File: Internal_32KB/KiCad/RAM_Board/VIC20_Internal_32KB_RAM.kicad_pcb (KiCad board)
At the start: 2 copper layers, 65 x 61 mm, 13 parts, among them J1 UD4, J2 UE4, J3 Switch, J4 RAM Decode, J5 BLK Inputs, J6 BLK Outputs, U1 62256, U2 RAM Decoder, U3 BLK Decoder

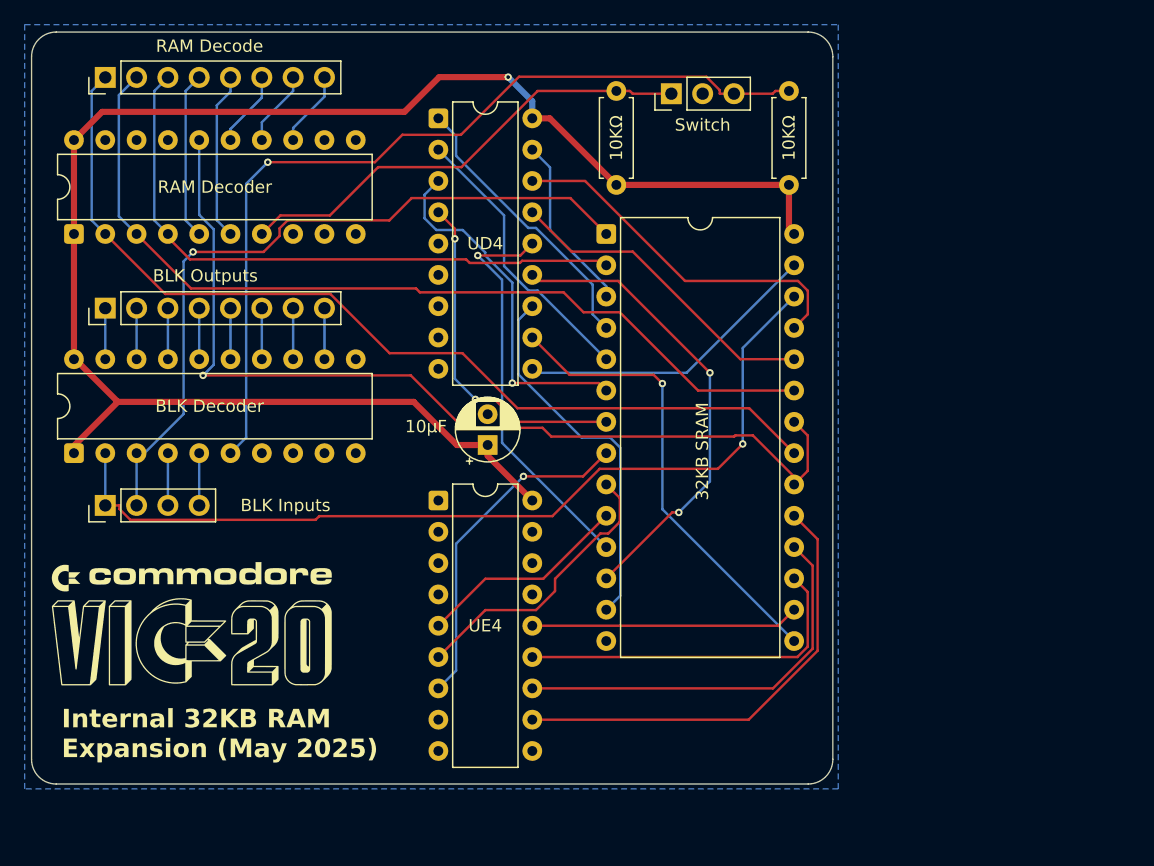
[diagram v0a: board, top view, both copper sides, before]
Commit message: Redesigned 32KB expansion
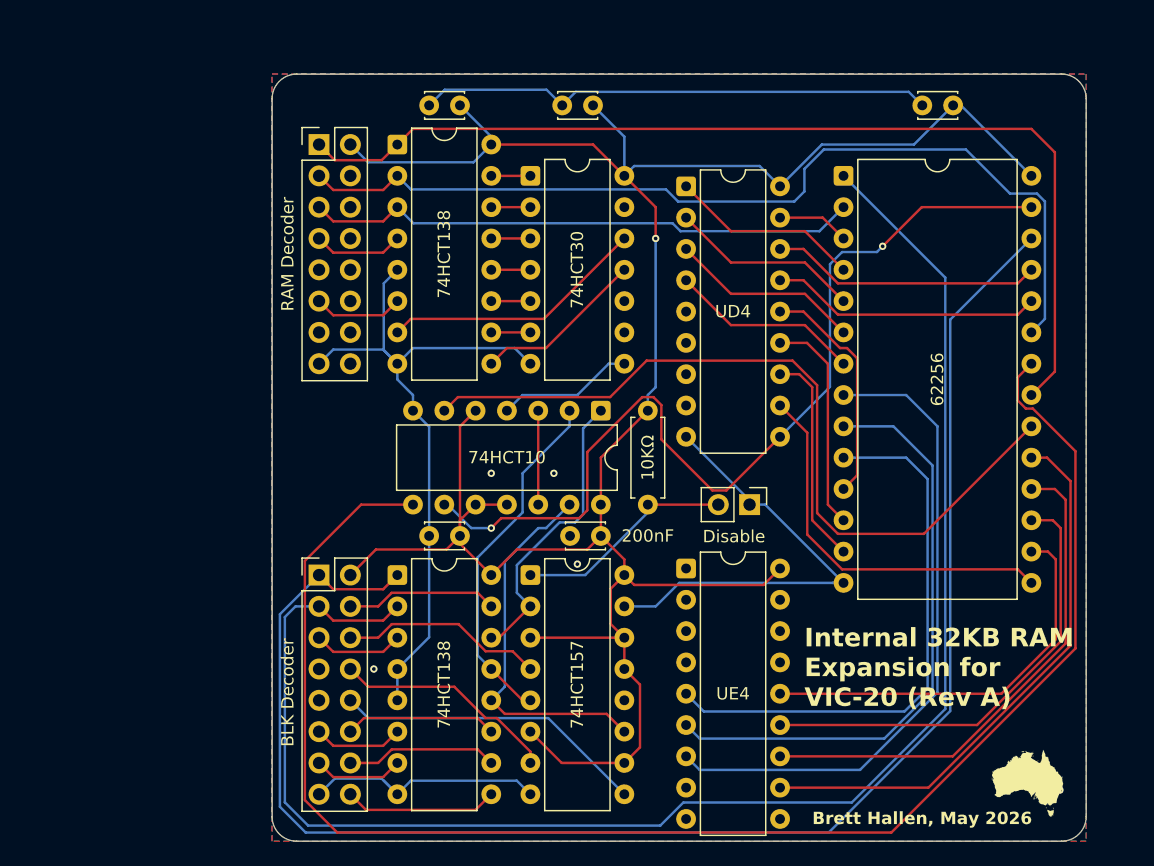
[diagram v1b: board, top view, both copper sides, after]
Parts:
- removed G***: LOGO, LOGO
- removed the J4 at (53.0, 31.8)
- removed the J5 at (53.0, 66.5)
- removed J6: BLK Outputs, Connector_PinHeader_2.54mm:PinHeader_1x08_P2.54mm_Vertical
- removed R2: 10KΩ, Resistor_THT:R_Axial_DIN0207_L6.3mm_D2.5mm_P7.62mm_Horizontal
- added C2: 100nF, Capacitor_THT:C_Disc_D3.0mm_W2.0mm_P2.50mm, F.Cu at (92.6, 34.1)
- added C3: 100nF, Capacitor_THT:C_Disc_D3.0mm_W2.0mm_P2.50mm, F.Cu at (121.8, 34.1)
- added C4: 100nF, Capacitor_THT:C_Disc_D3.0mm_W2.0mm_P2.50mm, F.Cu at (81.8, 69.0)
- added C5: 200nF, Capacitor_THT:C_Disc_D3.0mm_W2.0mm_P2.50mm, F.Cu at (93.2, 69.0)
- added J1: BLK Decoder, Connector_PinHeader_2.54mm:PinHeader_2x08_P2.54mm_Vertical, F.Cu at (70.4, 72.2)
- added J2: RAM Decoder, Connector_PinHeader_2.54mm:PinHeader_2x08_P2.54mm_Vertical, F.Cu at (70.4, 37.2)
- added U1: 74HCT138, Package_DIP:DIP-16_W7.62mm, F.Cu at (76.7, 72.2)
- added U4: 74HCT30, Package_DIP:DIP-14_W7.62mm, F.Cu at (87.5, 39.8)
- added U5: 74HCT157, Package_DIP:DIP-16_W7.62mm, F.Cu at (87.5, 72.2)
- C1: value 10µF -> 100nF; footprint Capacitor_THT:CP_Radial_D5.0mm_P2.50mm -> Capacitor_THT:C_Disc_D3.0mm_W2.0mm_P2.50mm
- J3: value Switch -> Disable/Enable Switch; footprint Connector_PinHeader_2.54mm:PinHeader_1x03_P2.54mm_Vertical -> Connector_PinHeader_2.54mm:PinHeader_1x02_P2.54mm_Vertical
- U2: value RAM Decoder -> 74HCT138; footprint Package_DIP:DIP-20_W7.62mm -> Package_DIP:DIP-16_W7.62mm
- U3: value BLK Decoder -> 74HCT10; footprint Package_DIP:DIP-20_W7.62mm -> Package_DIP:DIP-14_W7.62mm
- moved U3 42.9 mm to (93.2, 58.8), turned to -90 degrees
- moved J3 33.9 mm to (105.3, 66.5), turned to -90 degrees
- moved C1 27.6 mm to (81.8, 34.1), turned to 180 degrees
- moved U2 27.2 mm to (76.7, 37.2), turned to 0 degrees
- moved J4 20.8 mm to (100.1, 40.6)
- moved J5 20.8 mm to (100.1, 71.6)
- moved U6 19.8 mm to (112.9, 39.8)
- moved R1 18.5 mm to (97.0, 58.8), turned to -90 degrees
- renumbered J1 to J4, J2 to J5, U1 to U6
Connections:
- net BD0 renamed /BD0
- net BD1 renamed /BD1
- net BD2 renamed /BD2
- net BD3 renamed /BD3
- net BD4 renamed /BD4
- net BD5 renamed /BD5
- net BD6 renamed /BD6
- net BD7 renamed /BD7
- net VA0 renamed /VA0
- net VA1 renamed /VA1
- net VA2 renamed /VA2
- net VA3 renamed /VA3
- net VA4 renamed /VA4
- net VA5 renamed /VA5
- net VA6 renamed /VA6
- net VA7 renamed /VA7
- net VA8 renamed /VA8
- net VA9 renamed /VA9
- J3 pad 1: S1 -> GND
- J3 pad 2: GND -> Net-(J3-Pin_2)
- J4 pad 10: VR/W -> /VR/~{W}
- R1 pad 2: S1 -> Net-(J3-Pin_2)
- U2 pad 1: +5V -> /VA10
- U2 pad 10: GND -> /~{RAM5}
- U2 pad 11: GND -> /~{RAM4}
- U2 pad 12: unconnected-(U2-IO8-Pad12) -> /~{RAM3}
- U2 pad 13: ~{RAM3} -> /~{RAM2}
- U2 pad 14: ~{RAM2} -> /~{RAM1}
- U2 pad 15: ~{RAM1} -> /~{RAM0}
- U2 pad 16: ~{CS1} -> +5V
- U2 pad 2: VA10 -> /VA11
- U2 pad 3: VA11 -> /VA12
- U2 pad 4: VA12 -> /~{BLK0}/~{G2A}
- U2 pad 5: VA13/G1 -> GND
- U2 pad 6: ~{BLK0}/~{G2A} -> /VA13/G1
- U2 pad 7: S1 -> /~{RAM7}
- U2 pad 8: unconnected-(U2-I8-Pad8) -> GND
- U2 pad 9: unconnected-(U2-I9-Pad9) -> /~{RAM6}
- U3 pad 1: +5V -> /~{BLK1}
- U3 pad 10: GND -> +5V
- U3 pad 11: GND -> +5V
- U3 pad 12: ~{BLK7} -> /~{BLK_CS}
- U3 pad 13: ~{BLK6} -> /~{BLK3}
- U3 pad 14: ~{BLK5} -> +5V
- U3 pad 2: CA13 -> /~{BLK2}
- U3 pad 3: CA14 -> /~{BLK_CS}
- U3 pad 4: CA15 -> /~{RAM_CS}
- U3 pad 5: SΦ2/G1 -> +5V
- U3 pad 6: S2 -> /~{CS}
- U3 pad 7: unconnected-(U3-I7-Pad7) -> GND
- U3 pad 8: unconnected-(U3-I8-Pad8) -> /~{OE}
- U3 pad 9: unconnected-(U3-I9-Pad9) -> /VR/~{W}
- U6 pad 1: CA14 -> /CA14
- U6 pad 2: VA12 -> /VA12
- U6 pad 20: ~{CS1} -> /~{CS}
- U6 pad 21: VA10 -> /VA10
- U6 pad 22: ~{CS1} -> /~{OE}
- U6 pad 23: VA11 -> /VA11
- U6 pad 26: CA13 -> /CA13
- U6 pad 27: VR/W -> /VR/~{W}
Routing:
- net GND: track 0.00 -> 157.1 mm, vias 0 -> 5
- net /CA14: track 0.00 -> 130.4 mm
- net /CA13: track 0.00 -> 127.8 mm
- net /~{OE}: track 0.00 -> 125.7 mm
- net /VA10: track 0.00 -> 82.5 mm
- net ~{CS1}: track 77.8 -> 0.00 mm, vias 1 -> 0
- net VA10: track 76.9 -> 0.00 mm
- net /VA11: track 0.00 -> 76.3 mm
- net /VR/~{W}: track 0.00 -> 75.7 mm, vias 0 -> 2
- net CA13: track 72.8 -> 0.00 mm, vias 1 -> 0
- net VA11: track 72.5 -> 0.00 mm
- net S2: track 70.8 -> 0.00 mm, vias 1 -> 0
- net +5V: track 134.6 -> 199.5 mm
- net /~{CS}: track 0.00 -> 64.8 mm
- net CA14: track 60.0 -> 0.00 mm, vias 1 -> 0
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- added copper zone on F.Cu, net GND
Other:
- board size 65 x 61 mm -> 66 x 62.2 mm
- board text added: "26-MAY-2026: Pending testing"
- board text added: "Brett Hallen, May 2026"
- board text added: "Disable"
- board text added: "Internal 32KB RAM Expansion for VIC-20 (Rev A)"
- board text removed: "32KB SRAM"
- board text removed: "Brett Hallen, May 2025 Port Macquarie, Australia www.youtube.com/@Brfff"
- board text removed: "Internal 32KB RAM Expansion (May 2025)"

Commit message: Silkscreen improvements
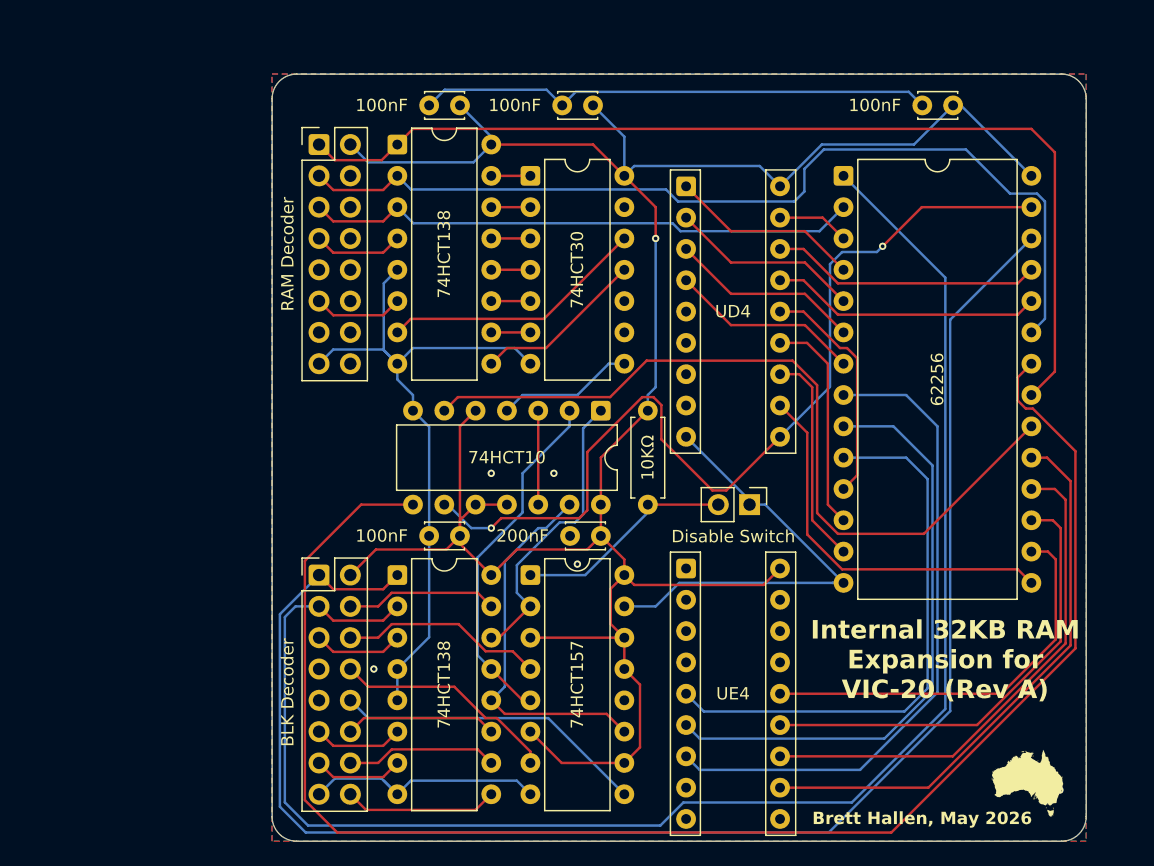
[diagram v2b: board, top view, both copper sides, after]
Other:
- board text added: "2114 SRAM Socket"
- board text added: "3-to-8 Decoder"
- board text added: "32KB SRAM"
- board text added: "8-Input NAND Gate"
- board text added: "Disable Switch"
- board text added: "Quad 2-Input Multiplexer"
- board text added: "To/From VIC"
- board text added: "Triple 3-Input NAND Gate"
- board text removed: "Disable"
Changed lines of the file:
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@@
 		)
 		(property "Value" "100nF"
-			(at 1.25 2.25 0)
-			(layer "F.Fab")
-			(hide yes)
+			(at 6.35 0 0)
+			(layer "F.SilkS")
 			(effects
 				(font
 					(size 1 1)
-					(thickness 0.15)
+					(thickness 0.125)
 				)
 			)
@@
 		)
 		(property "Value" "100nF"
-			(at 1.25 2.25 0)
-			(layer "F.Fab")
-			(hide yes)
+			(at 6.35 0 0)
+			(layer "F.SilkS")
 			(effects
 				(font
 					(size 1 1)
-					(thickness 0.15)
+					(thickness 0.125)
 				)
 			)
@@
 	)
 	(footprint "Package_DIP:DIP-18_W7.62mm"
-		(locked yes)
 		(layer "F.Cu")
 		(at 100.137 71.635)
@@
 		(attr through_hole)
 		(fp_line
+			(start -1.27 -1.33)
+			(end -1.27 21.65)
+			(stroke
+				(width 0.12)
+				(type solid)
+			)
+			(layer "F.SilkS")
+		)
+		(fp_line
+			(start 1.16 -1.33)
+			(end -1.27 -1.33)
+			(stroke
+				(width 0.12)
+				(type solid)
+			)
+			(layer "F.SilkS")
+		)
+		(fp_line
 			(start 1.16 -1.33)
 			(end 1.16 21.65)
@@
 		(fp_line
 			(start 1.16 21.65)
-			(end 6.46 21.65)
+			(end -1.27 21.65)
 			(stroke
 				(width 0.12)
@@
 		)
 		(fp_line
-			(start 2.81 -1.33)
-			(end 1.16 -1.33)
+			(start 6.46 21.65)
+			(end 6.46 -1.33)
 			(stroke
 				(width 0.12)
@@
 		)
 		(fp_line
-			(start 6.46 -1.33)
-			(end 4.81 -1.33)
+			(start 8.89 -1.33)
+			(end 6.46 -1.33)
 			(stroke
 				(width 0.12)
@@
 		)
 		(fp_line
-			(start 6.46 21.65)
-			(end 6.46 -1.33)
+			(start 8.89 21.65)
+			(end 6.46 21.65)
 			(stroke
 				(width 0.12)
@@
 			(layer "F.SilkS")
 		)
-		(fp_arc
-			(start 4.81 -1.33)
-			(mid 3.81 -0.33)
-			(end 2.81 -1.33)
+		(fp_line
+			(start 8.89 21.65)
+			(end 8.89 -1.33)
 			(stroke
 				(width 0.12)
@@
 		)
 		(property "Value" "100nF"
-			(at 1.25 2.25 0)
-			(layer "F.Fab")
-			(hide yes)
+			(at 6.35 0 0)
+			(layer "F.SilkS")
 			(effects
 				(font
 					(size 1 1)
-					(thickness 0.15)
+					(thickness 0.125)
 				)
 			)
@@
 	)
 	(footprint "Package_DIP:DIP-18_W7.62mm"
-		(locked yes)
 		(layer "F.Cu")
 		(at 100.137 40.635)
@@
 		(attr through_hole)
 		(fp_line
+			(start -1.27 -1.33)
+			(end -1.27 21.65)
+			(stroke
+				(width 0.12)
+				(type solid)
+			)
+			(layer "F.SilkS")
+		)
+		(fp_line
+			(start 1.16 -1.33)
+			(end -1.27 -1.33)
+			(stroke
+				(width 0.12)
+				(type solid)
+			)
+			(layer "F.SilkS")
+		)
+		(fp_line
 			(start 1.16 -1.33)
 			(end 1.16 21.65)
@@
 		(fp_line
 			(start 1.16 21.65)
-			(end 6.46 21.65)
+			(end -1.27 21.65)
 			(stroke
 				(width 0.12)
@@
 		)
 		(fp_line
-			(start 2.81 -1.33)
-			(end 1.16 -1.33)
+			(start 6.46 21.65)
+			(end 6.46 -1.33)
 			(stroke
 				(width 0.12)
@@
 		)
 		(fp_line
-			(start 6.46 -1.33)
-			(end 4.81 -1.33)
+			(start 8.89 -1.33)
+			(end 6.46 -1.33)
 			(stroke
 				(width 0.12)
@@
 		)
 		(fp_line
-			(start 6.46 21.65)
-			(end 6.46 -1.33)
+			(start 8.89 21.65)
+			(end 6.46 21.65)
 			(stroke
 				(width 0.12)
@@
 			(layer "F.SilkS")
 		)
-		(fp_arc
-			(start 4.81 -1.33)
-			(mid 3.81 -0.33)
-			(end 2.81 -1.33)
+		(fp_line
+			(start 8.89 21.65)
+			(end 8.89 -1.33)
 			(stroke
 				(width 0.12)
@@
 			)
 		)
-		(pad "1" thru_hole rect
+		(pad "1" thru_hole roundrect
 			(at 0 0)
 			(size 1.7 1.7)
@@
 			(layers "*.Cu" "*.Mask")
 			(remove_unused_layers no)
+			(roundrect_rratio 0.1470588235)
 			(net 12 "/CA13")
 			(pinfunction "Pin_1")
@@
 			)
 		)
-		(pad "1" thru_hole rect
+		(pad "1" thru_hole roundrect
 			(at 0 0)
 			(size 1.7 1.7)
@@
 			(layers "*.Cu" "*.Mask")
 			(remove_unused_layers no)
+			(roundrect_rratio 0.1470588235)
 			(net 18 "/VA10")
 			(pinfunction "Pin_1")
@@
 		)
 		(property "Value" "200nF"
-			(at -3.81 0 0)
+			(at 6.35 0 0)
 			(layer "F.SilkS")
 			(effects
@@
 		)
 		(property "Value" "100nF"
-			(at 1.25 2.25 0)
-			(layer "F.Fab")
-			(hide yes)
+			(at 6.35 0 0)
+			(layer "F.SilkS")
 			(effects
 				(font
 					(size 1 1)
-					(thickness 0.15)
+					(thickness 0.125)
 				)
 			)
@@
 		(layer "Edge.Cuts")
 	)
-	(gr_text "Disable"
-		(at 101.477 69.63 0)
+	(gr_text "Disable Switch"
+		(at 98.937 69.63 0)
 		(layer "F.SilkS")
 		(effects
@@
 	)
 	(gr_text "Internal 32KB RAM \nExpansion for \nVIC-20 (Rev A)"
-		(at 109.732 82.965 0)
+		(at 121.162 82.33 0)
 		(layer "F.SilkS")
 		(effects
@@
 				(bold yes)
 			)
-			(justify left bottom)
+			(justify bottom)
+		)
+	)
+	(gr_text "Triple 3-Input NAND Gate"
+		(at 95.127 63.28 0)
+		(layer "B.SilkS")
+		(effects
+			(font
+				(size 1 1)
+				(thickness 0.1)
+			)
+			(justify left bottom mirror)
+		)
+	)
+	(gr_text "To/From VIC"
+		(at 68.457 41.69 90)
+		(layer "B.SilkS")
+		(effects
+			(font
+				(size 1 1)
+				(thickness 0.1)
+			)
+			(justify left bottom mirror)
+		)
+	)
+	(gr_text "To/From VIC"
+		(at 68.457 76.615 90)
+		(layer "B.SilkS")
+		(effects
+			(font
+				(size 1 1)
+				(thickness 0.1)
+			)
+			(justify left bottom mirror)
+		)
+	)
+	(gr_text "3-to-8 Decoder"
+		(at 81.157 40.42 90)
+		(layer "B.SilkS")
+		(effects
+			(font
+				(size 1 1)
+				(thickness 0.1)
+			)
+			(justify left bottom mirror)
+		)
+	)
+	(gr_text "3-to-8 Decoder"
+		(at 81.157 74.71 90)
+		(layer "B.SilkS")
+		(effects
+			(font
+				(size 1 1)
+				(thickness 0.1)
+			)
+			(justify left bottom mirror)
+		)
+	)
+	(gr_text "8-Input NAND Gate"
+		(at 91.952 40.42 90)
+		(layer "B.SilkS")
+		(effects
+			(font
+				(size 1 1)
+				(thickness 0.1)
+			)
+			(justify left bottom mirror)
+		)
+	)
+	(gr_text "Quad 2-Input Multiplexer"
+		(at 91.952 71.535 90)
+		(layer "B.SilkS")
+		(effects
+			(font
+				(size 1 1)
+				(thickness 0.1)
+			)
+			(justify left bottom mirror)
+		)
+	)
+	(gr_text "2114 SRAM Socket"
+		(at 104.652 43.595 90)
+		(layer "B.SilkS")
+		(effects
+			(font
+				(size 1 1)
+				(thickness 0.1)
+			)
+			(justify left bottom mirror)
+		)
+	)
+	(gr_text "2114 SRAM Socket"
+		(at 104.652 74.71 90)
+		(layer "B.SilkS")
+		(effects
+			(font
+				(size 1 1)
+				(thickness 0.1)
+			)
+			(justify left bottom mirror)
+		)
+	)
+	(gr_text "32KB SRAM"
+		(at 121.162 51.85 90)
+		(layer "B.SilkS")
+		(effects
+			(font
+				(size 1 1)
+				(thickness 0.1)
+			)
+			(justify left bottom mirror)
 		)
 	)
